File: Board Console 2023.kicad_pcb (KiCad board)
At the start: 6 copper layers, 214.2 x 98 mm, 204 parts, among them J1 Raspberry PI, J10 I2C_Conn, J11 USB_C, J13 SpeakerL, J14 SpeakerR, J15 Rasp_HDMI, J16 HDMI_OUT, J17 TTL 40Pin, J18 I2C EDID, J2 Composite OUT, J3 L1/L2, J4 SJ1-3525N, J5 USB_B_Micro, J6 Display, J7 USB_A, J8 R1/R2, J9 V_BATT, SW10 A, SW11 X, SW12 Down, SW13 Left, SW14 Up, SW15 Right, SW16 PWR_Push, SW17 SuperDX, SW3 Vol -, SW4 SuperSX, SW5 Select, SW6 Vol +, SW7 Start, SW8 B, SW9 Y, U1 MP3438GTL-P, U10 TS3DV642A0RUAR, U11 LM1117DT-3.3, U12 FAN5333BSX, U13 TFP401APZPR, U14 24LC02BT-E/LT, U15 LTC2950CTS8-1-TRMPBF, U2 MP3421GG-Z, U3 LM1117DT-3.3, U4 MP2722GRH-0000-P, U5 ADS1115IDGS, U6 NC7WV16P6X, U7 PAM8302AAD, U8 PAM8302AAD, U9 LM1117DT-3.3

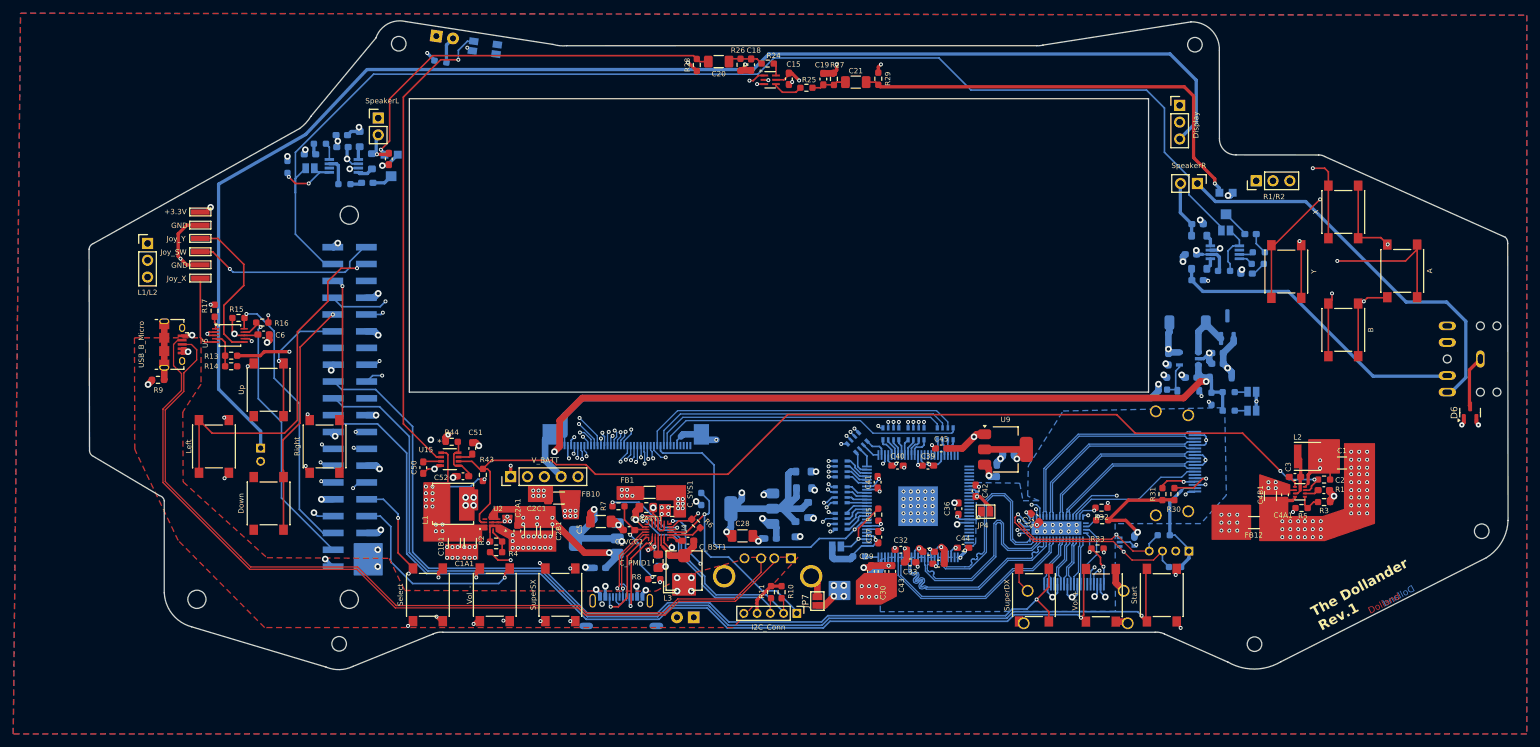
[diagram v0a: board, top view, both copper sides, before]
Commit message: aggiunto pin enable switch per schermo composito
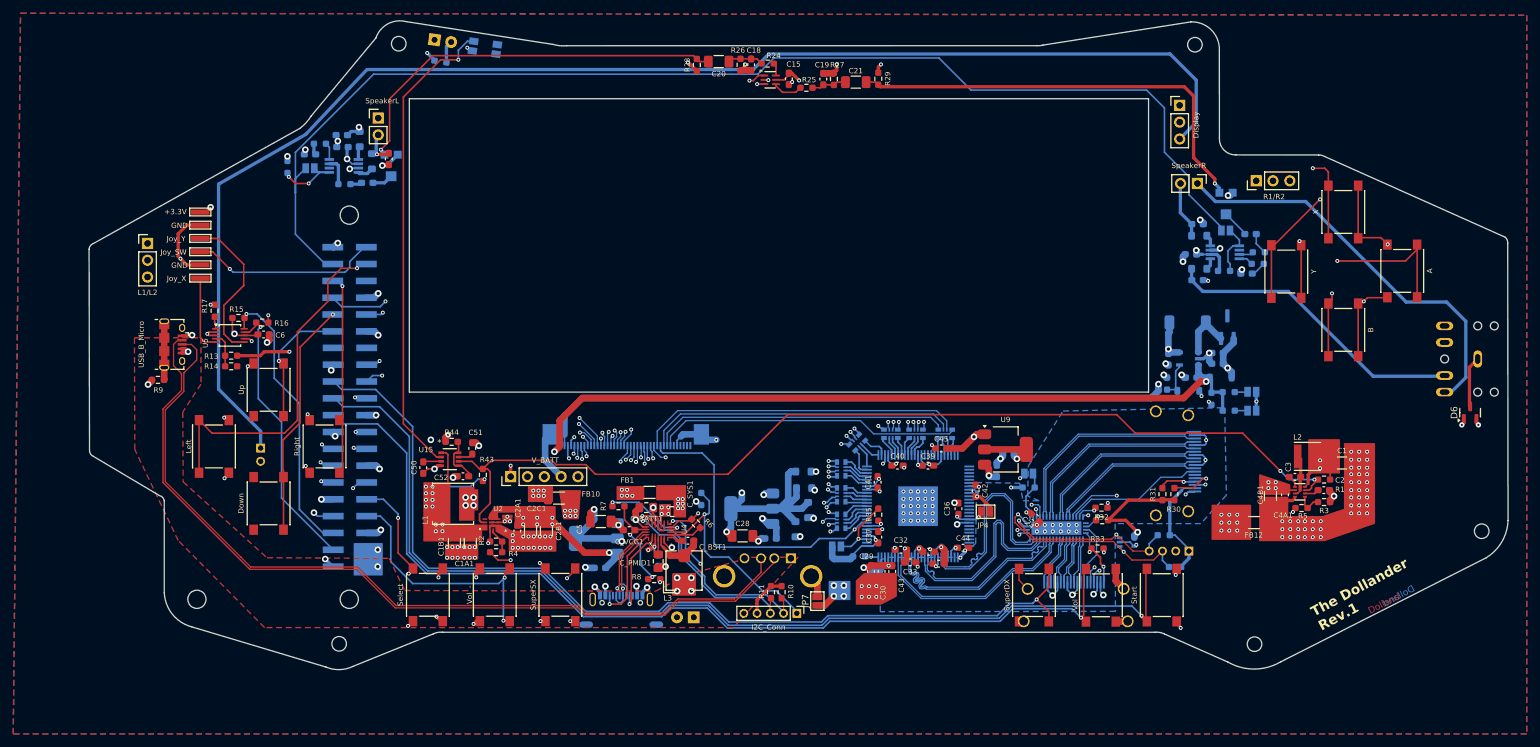
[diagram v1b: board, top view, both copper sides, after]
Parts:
- added JP8: SJ, Jumper:SolderJumper-2_P1.3mm_Open_Pad1.0x1.5mm, B.Cu at (180.4, 110.5)
- added R46: 10k, Resistor_SMD:R_0603_1608Metric_Pad0.98x0.95mm_HandSolder, B.Cu at (180.4, 112.6)
- RN1, RN2, RN3, RN4, RN5, RN6, RN7: footprint Resistor_SMD:R_Array_Convex_4x0603 -> EXB28V330JX:EXB28V_PAN
- moved D5 0.61 mm to (90.7, 45.0)
- moved J4 0.40 mm to (248.2, 93.2)
- moved J16 0.30 mm to (187.5, 131.9)
- moved J11 0.20 mm to (118.9, 132.6)
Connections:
- J1 pad 22: unconnected-(J1-Pin_22-Pad22) -> EN_Switch
- U10 pad 2: /HDMI Switch/+3.3V -> Net-(JP8-B)
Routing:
- net EN_Switch: track 0.00 -> 135.5 mm, vias 0 -> 2
- net Net-(JP8-B): track 0.00 -> 7.66 mm
- net GND: track 251.3 -> 250.2 mm
- net Net-(D5-A): track 4.05 -> 3.39 mm
- net GNDPWR: track 7.76 -> 8.32 mm
- net /HDMI Switch/+3.3V: track 38.6 -> 39.0 mm, vias 3 -> 4
